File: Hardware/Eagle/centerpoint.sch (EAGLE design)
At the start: 5 parts, among them M1 ARDUINO-NANO-3.0

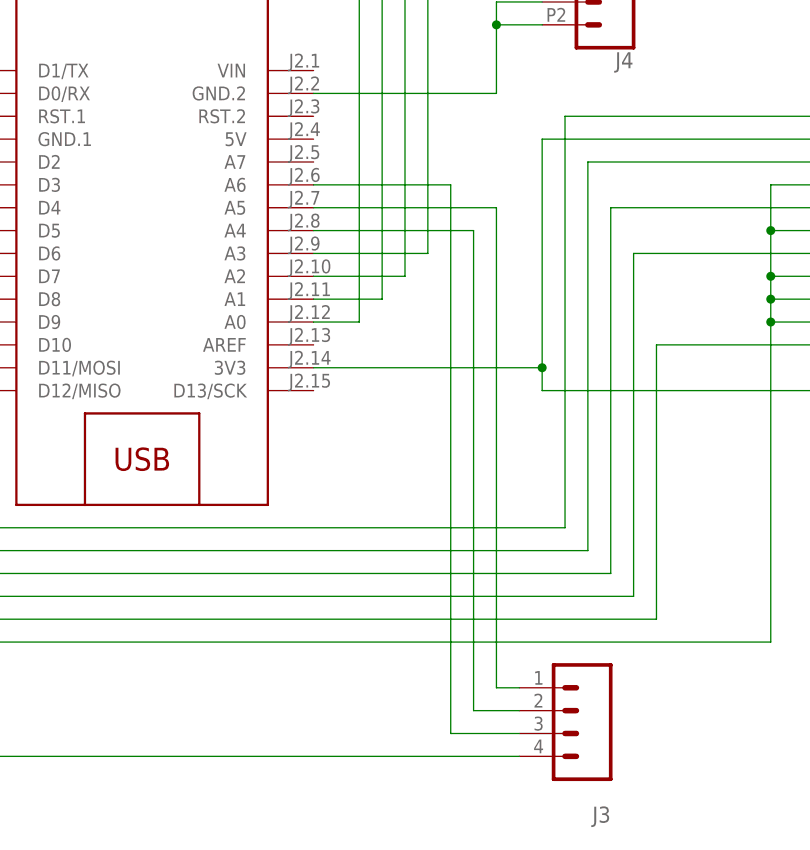
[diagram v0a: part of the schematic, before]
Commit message: updated adapter board PCB layout
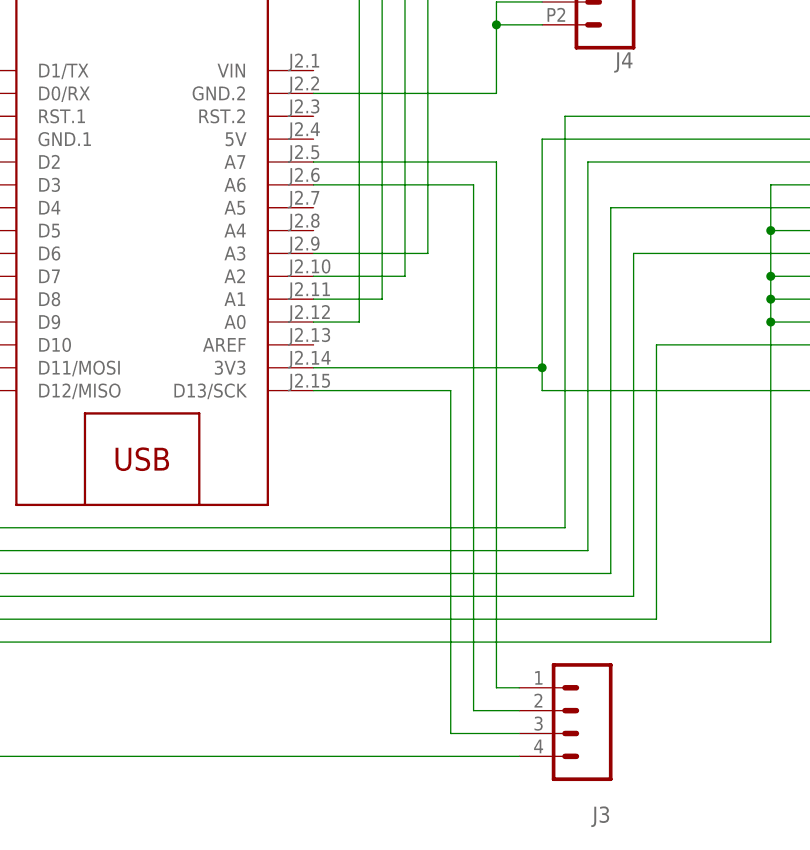
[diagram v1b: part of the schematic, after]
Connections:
- net N$17: now also J3.1, M1.A7; no longer J3.3, M1.A6
- net N$18: now also J3.2, M1.A6; no longer J3.1, M1.A5
- net N$19: now also J3.3, M1.D13/SCK; no longer J3.2, M1.A4
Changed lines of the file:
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@@
-</segment>
-</net>
-<net name="N$17" class="0">
-<segment>
-<pinref part="M1" gate="G$1" pin="A6"/>
-<wire x1="134.62" y1="38.1" x2="149.86" y2="38.1" width="0.1524" layer="91"/>
-<wire x1="149.86" y1="38.1" x2="149.86" y2="-22.86" width="0.1524" layer="91"/>
-<pinref part="J3" gate="J1" pin="3"/>
-<wire x1="149.86" y1="-22.86" x2="157.48" y2="-22.86" width="0.1524" layer="91"/>
-</segment>
-</net>
-<net name="N$19" class="0">
-<segment>
-<pinref part="J3" gate="J1" pin="2"/>
-<wire x1="152.4" y1="-20.32" x2="157.48" y2="-20.32" width="0.1524" layer="91"/>
-<pinref part="M1" gate="G$1" pin="A4"/>
-<wire x1="152.4" y1="-20.32" x2="152.4" y2="33.02" width="0.1524" layer="91"/>
-<wire x1="152.4" y1="33.02" x2="134.62" y2="33.02" width="0.1524" layer="91"/>
-</segment>
-</net>
-<net name="N$18" class="0">
-<segment>
-<pinref part="M1" gate="G$1" pin="A5"/>
-<wire x1="134.62" y1="35.56" x2="154.94" y2="35.56" width="0.1524" layer="91"/>
-<pinref part="J3" gate="J1" pin="1"/>
-<wire x1="154.94" y1="35.56" x2="154.94" y2="-17.78" width="0.1524" layer="91"/>
-<wire x1="154.94" y1="-17.78" x2="157.48" y2="-17.78" width="0.1524" layer="91"/>
 </segment>
 </net>
@@
 </segment>
 </net>
+<net name="N$17" class="0">
+<segment>
+<pinref part="M1" gate="G$1" pin="A7"/>
+<wire x1="134.62" y1="40.64" x2="154.94" y2="40.64" width="0.1524" layer="91"/>
+<pinref part="J3" gate="J1" pin="1"/>
+<wire x1="154.94" y1="40.64" x2="154.94" y2="-17.78" width="0.1524" layer="91"/>
+<wire x1="154.94" y1="-17.78" x2="157.48" y2="-17.78" width="0.1524" layer="91"/>
+</segment>
+</net>
+<net name="N$18" class="0">
+<segment>
+<pinref part="M1" gate="G$1" pin="A6"/>
+<wire x1="134.62" y1="38.1" x2="152.4" y2="38.1" width="0.1524" layer="91"/>
+<pinref part="J3" gate="J1" pin="2"/>
+<wire x1="152.4" y1="38.1" x2="152.4" y2="-20.32" width="0.1524" layer="91"/>
+<wire x1="152.4" y1="-20.32" x2="157.48" y2="-20.32" width="0.1524" layer="91"/>
+</segment>
+</net>
+<net name="N$19" class="0">
+<segment>
+<pinref part="M1" gate="G$1" pin="D13/SCK"/>
+<wire x1="134.62" y1="15.24" x2="149.86" y2="15.24" width="0.1524" layer="91"/>
+<pinref part="J3" gate="J1" pin="3"/>
+<wire x1="149.86" y1="15.24" x2="149.86" y2="-22.86" width="0.1524" layer="91"/>
+<wire x1="149.86" y1="-22.86" x2="157.48" y2="-22.86" width="0.1524" layer="91"/>
+</segment>
+</net>

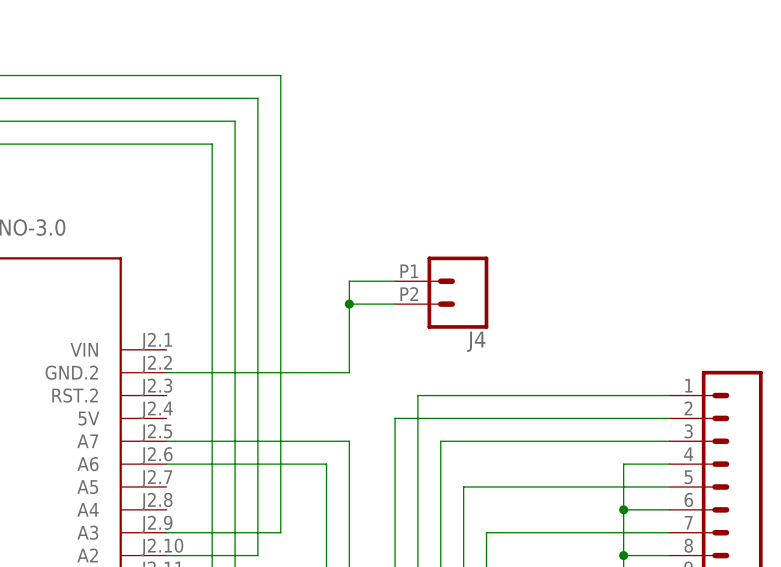
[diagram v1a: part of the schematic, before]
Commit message: added to silkscreen, change from 2.54 to 5mm screw terminal
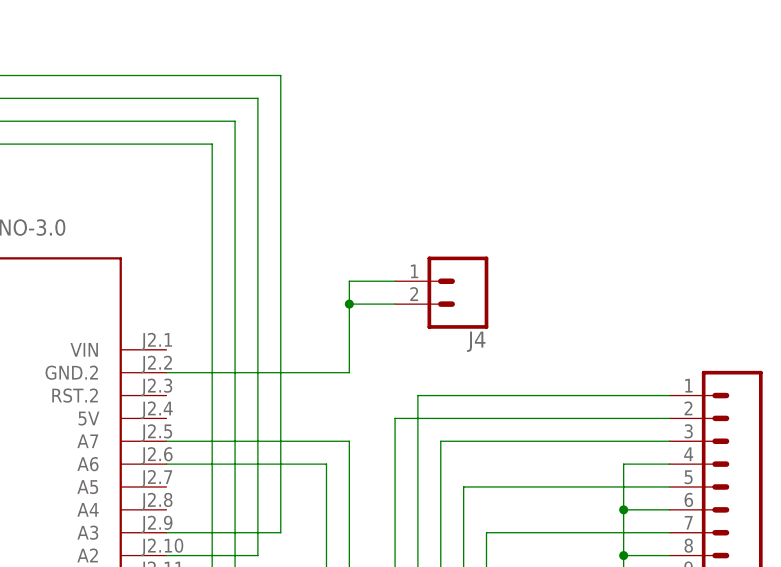
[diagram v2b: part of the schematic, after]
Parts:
- J4: device SparkFun-Connectors:CONN_022.54MM_SCREWTERM -> SparkFun-Connectors:CONN_023.5MM
